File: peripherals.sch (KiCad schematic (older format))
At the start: 21 parts

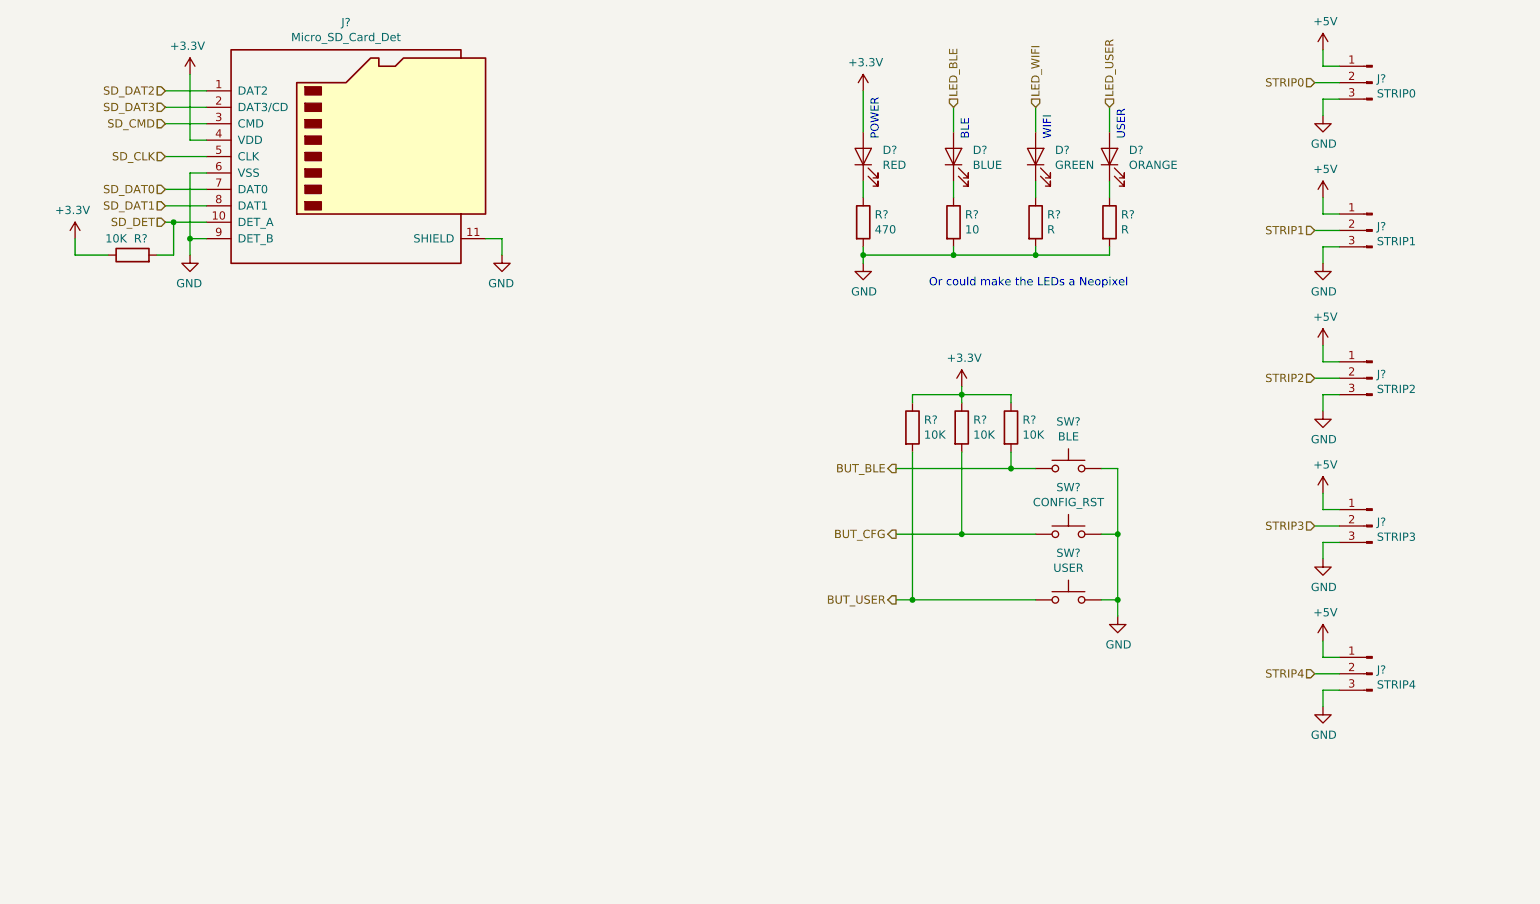
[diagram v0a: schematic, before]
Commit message: Added a level shifter and removed a channel
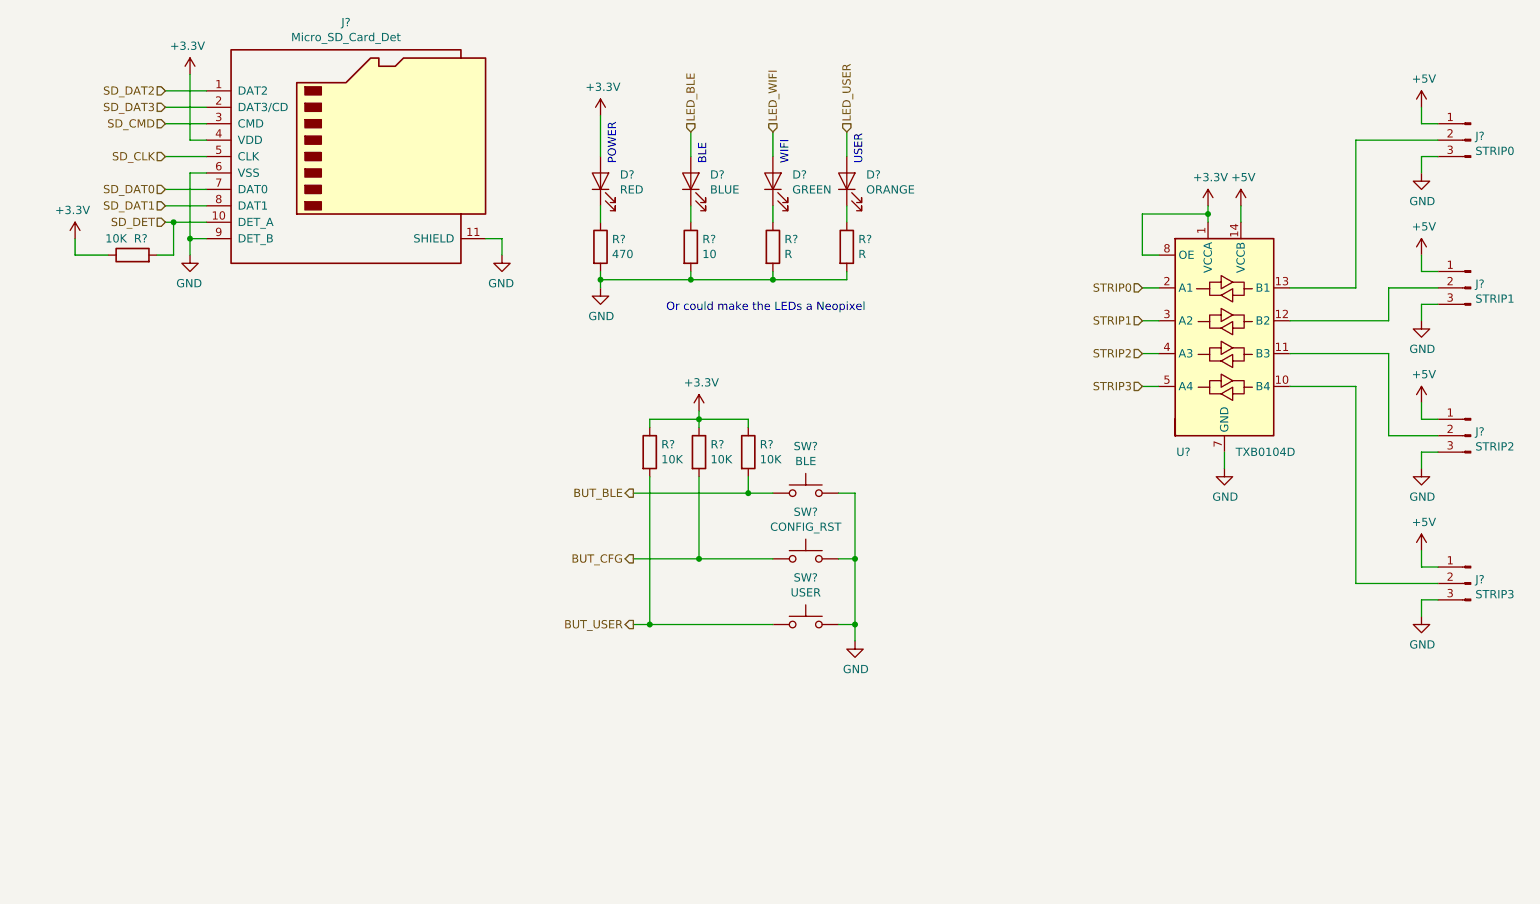
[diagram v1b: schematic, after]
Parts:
- removed J?: STRIP4, Connector_PinHeader_2.54mm:PinHeader_1x03_P2.54mm_Vertical, symbol Connector:Conn_01x03_Male
- added U?: TXB0104D, Package_SO:SOIC-14_3.9x8.7mm_P1.27mm, symbol Logic_LevelTranslator:TXB0104D
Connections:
- net +3V3: now also U?.1 (VCCA), U?.8 (OE)
- net +5V: now also U?.14 (VCCB)
- net GND: now also U?.7 (GND)
- net STRIP0: now also U?.2 (A1); no longer J?.2 (Pin_2)
- net STRIP1: now also U?.3 (A2); no longer J?.2 (Pin_2)
- net STRIP2: now also U?.4 (A3); no longer J?.2 (Pin_2)
- net STRIP3: now also U?.5 (A4); no longer J?.2 (Pin_2)
- new net: J?.2 (Pin_2), U?.13 (B1)
- new net: J?.2 (Pin_2), U?.12 (B2)
- new net: J?.2 (Pin_2), U?.11 (B3)
- new net: J?.2 (Pin_2), U?.10 (B4)
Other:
- moved on the sheet: D?, J?, R?, SW?

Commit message: About to change the entire damn thing to handle more current
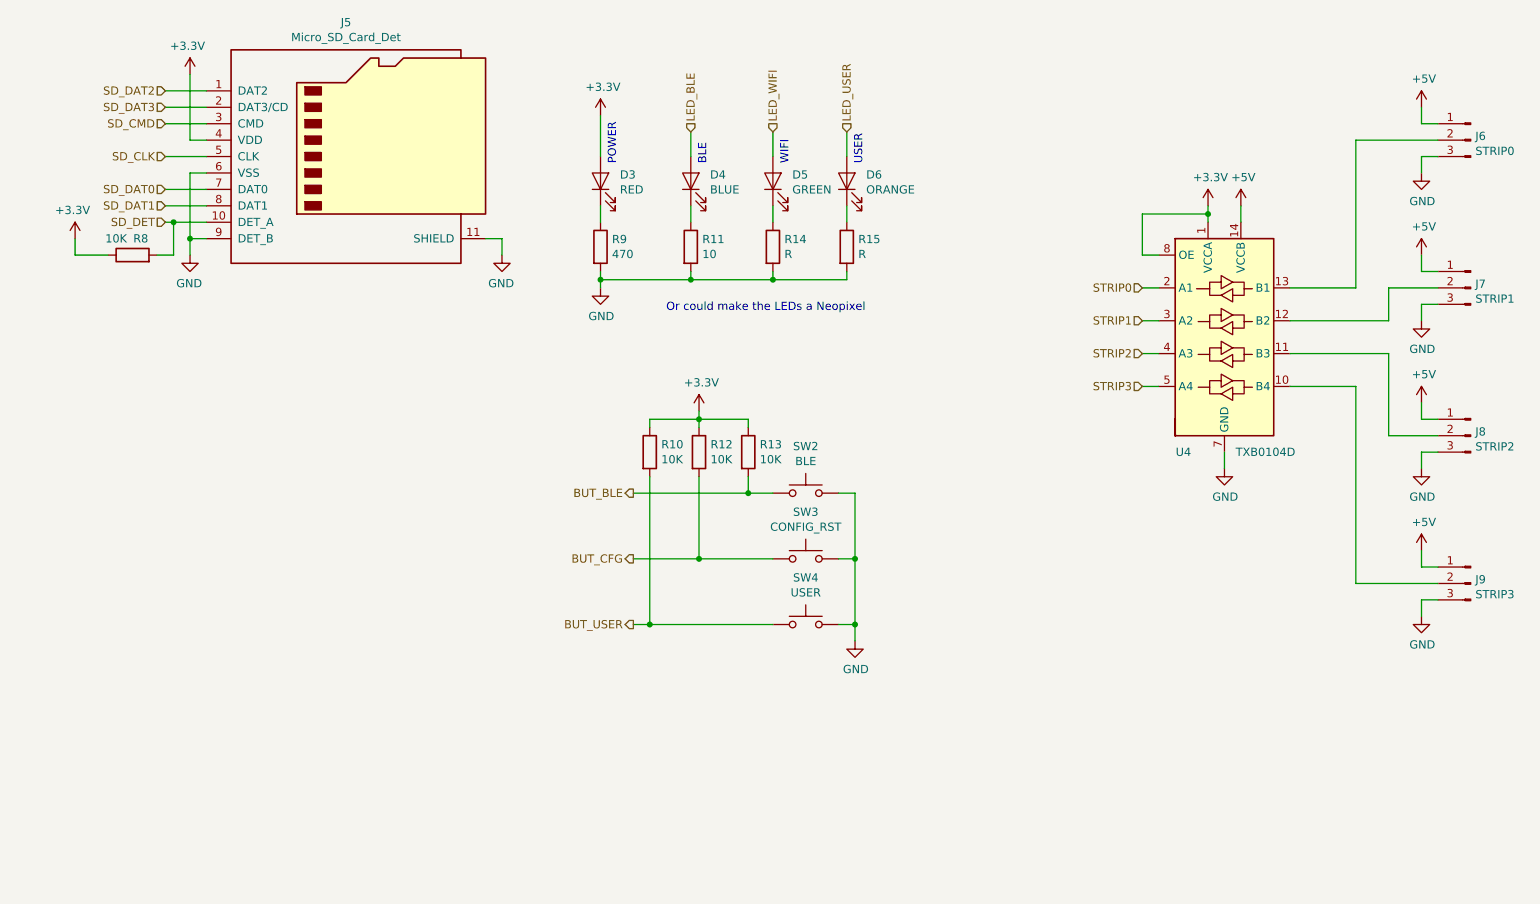
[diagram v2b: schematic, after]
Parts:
- D3, D4, D5, D6: renamed from D?; footprint (none) -> LED_SMD:LED_1206_3216Metric
- J5: renamed from J?; footprint (none) -> Connector_Card:microSD_HC_Hirose_DM3D-SF
- R10, R11, R12, R13, R14, R15, R8, R9: renamed from R?; footprint (none) -> Resistor_SMD:R_0805_2012Metric
- SW2: renamed from SW?; footprint (none) -> Button_Switch_SMD:SW_Push_1P1T_NO_CK_KMR2
- SW3, SW4: renamed from SW?; footprint CONFIG_RST -> Button_Switch_SMD:SW_Push_1P1T_NO_CK_KMR2
- gave numbers to parts that had none: 5

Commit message: Ordered files
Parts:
- removed U4: TXB0104D, Package_SO:SOIC-14_3.9x8.7mm_P1.27mm, symbol Logic_LevelTranslator:TXB0104D
- added C13: 1uF, Capacitor_SMD:C_0805_2012Metric, symbol Device:C
- added J10: STRIP4, Connector_PinHeader_2.54mm:PinHeader_1x03_P2.54mm_Vertical, symbol Connector:Conn_01x03_Male
- added J11: STRIP5, Connector_PinHeader_2.54mm:PinHeader_1x03_P2.54mm_Vertical, symbol Connector:Conn_01x03_Male
- added J12: STRIP6, Connector_PinHeader_2.54mm:PinHeader_1x03_P2.54mm_Vertical, symbol Connector:Conn_01x03_Male
- added J13: STRIP7, Connector_PinHeader_2.54mm:PinHeader_1x03_P2.54mm_Vertical, symbol Connector:Conn_01x03_Male
- added U4: 74HCT245, Package_SO:TSSOP-20_4.4x6.5mm_P0.65mm, symbol dot:74HCT245
- J5: footprint Connector_Card:microSD_HC_Hirose_DM3D-SF -> Connector_Card:microSD_HC_Hirose_DM3BT-DSF-PEJS
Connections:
- net +3V3: now also C13.1
- net +5V: now also J10.1 (Pin_1), J11.1 (Pin_1), J12.1 (Pin_1), J13.1 (Pin_1), U4.1 (DIR), U4.20 (VCC)
- net GND: now also C13.2, J10.3 (Pin_3), J11.3 (Pin_3), J12.3 (Pin_3), J13.3 (Pin_3), U4.10 (GND), U4.19 (OUTE)
- net STRIP0: now also U4.9 (A8)
- net STRIP1: now also U4.8 (A7)
- net STRIP2: now also U4.7 (A6)
- net STRIP3: now also U4.6 (A5)
- net at J6.2 (Pin_2): now also U4.18 (B1)
- net at J7.2 (Pin_2): now also U4.17 (B2)
- net at J8.2 (Pin_2): now also U4.16 (B3)
- net at J9.2 (Pin_2): now also U4.15 (B4)
- new net: J10.2 (Pin_2), U4.14 (B5)
- new net: J11.2 (Pin_2), U4.13 (B6)
- new net: J12.2 (Pin_2), U4.12 (B7)
- new net: J13.2 (Pin_2), U4.11 (B8)
- new net STRIP4: U4.5 (A4)
- new net STRIP5: U4.4 (A3)
- new net STRIP6: U4.3 (A2)
- new net STRIP7: U4.2 (A1)
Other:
- moved on the sheet: D3, D4, D5, D6, J5, J6, J7, J8, J9, R10, R11, R12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

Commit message: Almost done with second rev
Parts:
- removed D6: ORANGE, LED_SMD:LED_1206_3216Metric, symbol Device:LED
- removed R10: 10K, Resistor_SMD:R_0805_2012Metric, symbol Device:R
- removed R15: R, Resistor_SMD:R_0805_2012Metric, symbol Device:R
- removed SW4: USER, Button_Switch_SMD:SW_Push_1P1T_NO_CK_KMR2, symbol Switch:SW_Push
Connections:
- net STRIP0: now also U4.2 (A1); no longer U4.9 (A8)
- net STRIP1: now also U4.3 (A2); no longer U4.8 (A7)
- net STRIP2: now also U4.4 (A3); no longer U4.7 (A6)
- net STRIP3: now also U4.5 (A4); no longer U4.6 (A5)
- net STRIP4: now also U4.6 (A5); no longer U4.5 (A4)
- net STRIP5: now also U4.7 (A6); no longer U4.4 (A3)
- net STRIP6: now also U4.8 (A7); no longer U4.3 (A2)
- net STRIP7: now also U4.9 (A8); no longer U4.2 (A1)
- net at J6.2 (Pin_2): now also U4.11 (B8); no longer U4.18 (B1)
- net at J7.2 (Pin_2): now also U4.12 (B7); no longer U4.17 (B2)
- net at J8.2 (Pin_2): now also U4.13 (B6); no longer U4.16 (B3)
- net at J10.2 (Pin_2): now also U4.15 (B4); no longer U4.14 (B5)
- net at J11.2 (Pin_2): now also U4.16 (B3); no longer U4.13 (B6)
- net at J12.2 (Pin_2): now also U4.17 (B2); no longer U4.12 (B7)
- net at J13.2 (Pin_2): now also U4.18 (B1); no longer U4.11 (B8)
- net at J9.2 (Pin_2): now also U4.14 (B5); no longer U4.15 (B4)
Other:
- note removed: "USER"
- moved on the sheet: J10, J11, J12, J13, J6, J7, J8, J9
